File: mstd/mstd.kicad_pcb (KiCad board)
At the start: 2 copper layers, 80 x 96.2 mm, 89 parts, among them J1 PROG, J2 Barrel_Jack, Q1 SI2301CDS-T1-GE3, Q2 2N7002, SW1 TSX101G100-250, U1 ICE40UP5K-SG48ITR, U10 74HCT05, U12 74HCT4066, U2 TLV70212DBVR, U3 TMI6050-33, U4 ESP32-WROOM-32E-N16, U5 74LVX3245MTCX, U6 74LVX3245MTCX, U7 SSD1306 OLED, U8 74HCT05, U9 APX803S-31SA

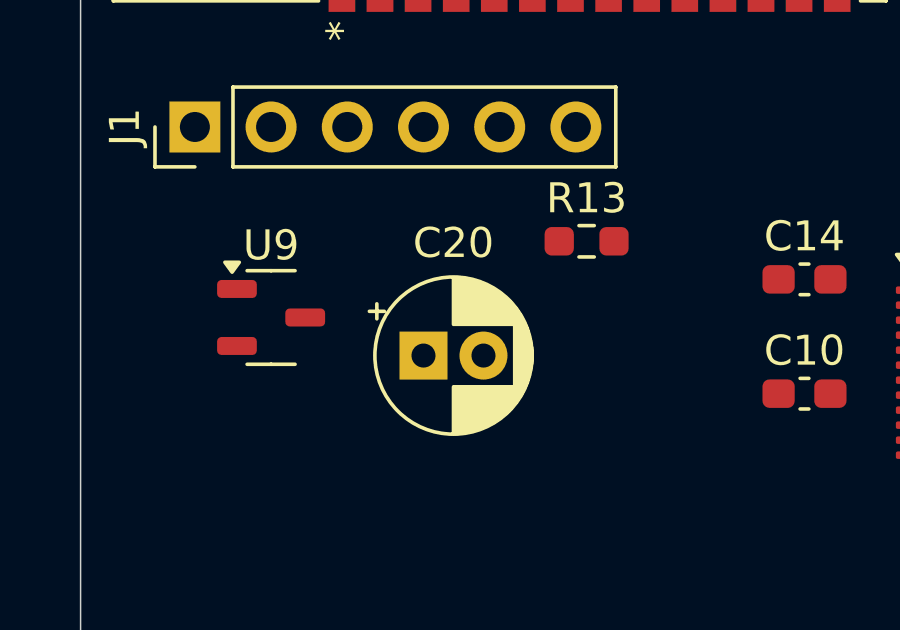
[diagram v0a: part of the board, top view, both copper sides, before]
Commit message: Changed reset capacitor to 1.0
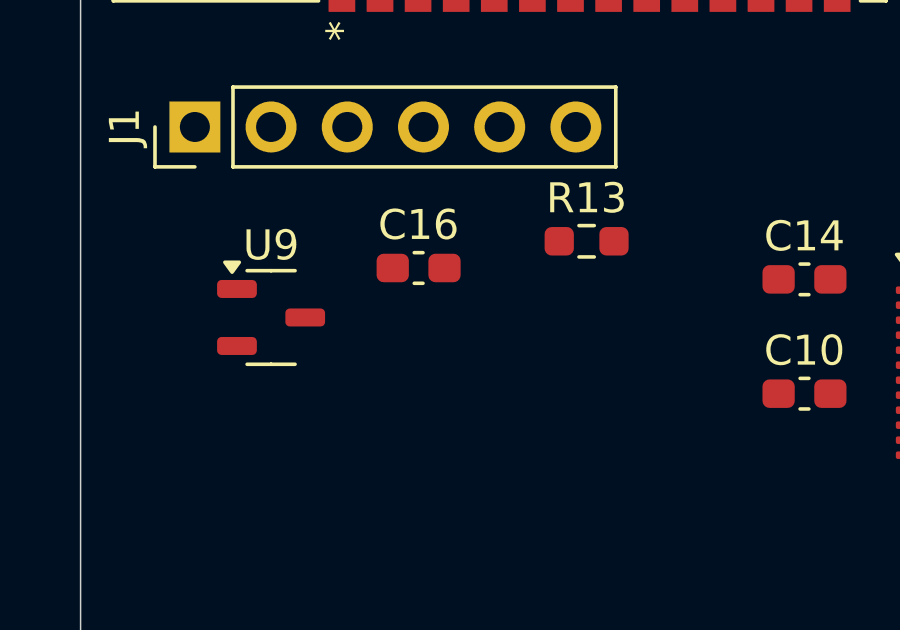
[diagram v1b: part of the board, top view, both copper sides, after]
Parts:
- removed C20: 10.0x16V, Capacitor_THT:CP_Radial_D5.0mm_P2.00mm
- added C16: 1.0, Capacitor_SMD:C_0603_1608Metric_Pad1.08x0.95mm_HandSolder, F.Cu at (63.3, 131.7)

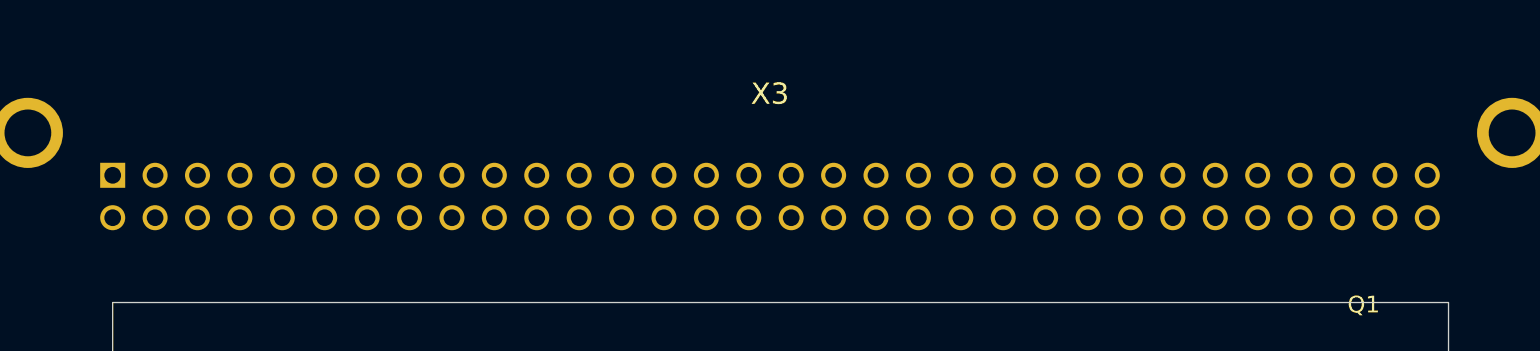
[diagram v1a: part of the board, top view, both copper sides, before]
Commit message: Update Harting connector pin numeration to match SNP
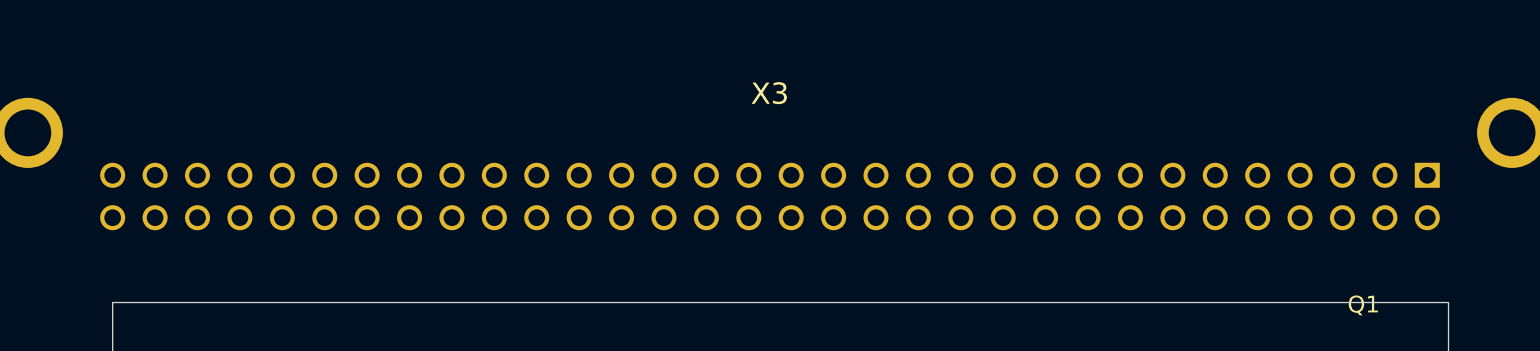
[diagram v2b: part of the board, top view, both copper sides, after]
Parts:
- X3: footprint local:09722642801 -> local:09722642801-1
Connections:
- X3 pad A32: unconnected-(X3D-ROM3-PadA32) -> (no net)
- X3 pad B32: /IO/DAL7 -> (no net)

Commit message: Routhing in finilizing stage
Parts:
- removed J2: Barrel_Jack, Connector_BarrelJack:BarrelJack_Wuerth_6941xx301002
- removed Q1: SI2301CDS-T1-GE3, easyeda2kicad:SOT-23-3_L3.0-W1.7-P0.95-LS2.9-BR
- removed R33: 1K, Resistor_SMD:R_0603_1608Metric_Pad0.98x0.95mm_HandSolder
- removed R34: 100K, Resistor_SMD:R_0603_1608Metric_Pad0.98x0.95mm_HandSolder
- added H1: MountingHole, MountingHole:MountingHole_3.2mm_M3_ISO14580, F.Cu at (116.8, 158.0)
- added H2: MountingHole, MountingHole:MountingHole_3.2mm_M3_ISO14580, F.Cu at (50.5, 101.1)
- added H3: MountingHole, MountingHole:MountingHole_3.2mm_M3_ISO14580, F.Cu at (139.6, 101.1)
- added H4: MountingHole, MountingHole:MountingHole_3.2mm_M3_ISO14580, F.Cu at (50.4, 168.5)
- added R40: 5K1, Resistor_SMD:R_0603_1608Metric_Pad0.98x0.95mm_HandSolder, F.Cu at (131.4, 143.2)
- added R41: 5K1, Resistor_SMD:R_0603_1608Metric_Pad0.98x0.95mm_HandSolder, F.Cu at (138.8, 142.3)
- added USB1: TYPEC-306DDW-ARP16, easyeda2kicad:USB-C-TH_TYPEC-306DDW-ARP16, F.Cu at (136.7, 142.7)
- C17, C22, C23, R3, R4, R5, R6, R7, R8, R9: moved to B.Cu
- moved R15 94.7 mm to (103.2, 110.2), turned to 180 degrees
- moved R30 91.9 mm to (101.3, 99.4), turned to 180 degrees
- moved R31 90.9 mm to (97.4, 99.4), turned to 180 degrees
- moved R32 90.0 mm to (67.1, 112.7), turned to 180 degrees
- moved R14 88.7 mm to (98.2, 110.8), turned to 90 degrees
- moved TP4 86.9 mm to (75.9, 112.7)
- moved TP3 83.6 mm to (75.9, 115.2)
- moved R29 80.2 mm to (92.2, 104.2), turned to 90 degrees
- moved TP2 80.0 mm to (76.9, 117.3)
- moved R19 77.3 mm to (89.9, 105.7), turned to -90 degrees
- moved R23 77.0 mm to (86.1, 112.1), turned to 180 degrees
- moved R16 75.2 mm to (98.2, 114.6), turned to -90 degrees
- moved C17 74.8 mm to (97.8, 104.6), turned to 180 degrees
- moved R28 73.2 mm to (90.5, 110.2), turned to -90 degrees
- moved R22 73.1 mm to (90.5, 121.0)
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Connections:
- R12 pad 1: /IO/ROM-CE3 -> /CE3
- R26 pad 1: /IO/WTB -> /WTB
- R28 pad 2: /IO/RUN -> /RUN
- R3 pad 1: /CPU/CIO7 -> /CPU/CIO2
- R32 pad 1: Net-(U1A-IOT_36b) -> /CPU/FIO4
- R4 pad 1: /CPU/CIO6 -> /CPU/CIO1
- R5 pad 1: /CPU/CIO0 -> /CPU/CI2
- R7 pad 1: /CPU/CI2 -> /CPU/CIO0
- SW1 pad 4: /CPU/CIO0 -> /CPU/CI2
- SW1 pad 6: /CPU/CI2 -> /CPU/CIO0
- TP1 pad 1: Net-(U1A-IOT_51a) -> Net-(U1A-IOT_36b)
- U1 pad 13: /CPU/FIO6 -> /RUN
- U1 pad 2: Net-(U1C-IOB_6a) -> /A6
- U1 pad 20: /CPU/FIO7 -> /CE3
- U1 pad 21: /CPU/FIO5 -> /WTB
- U1 pad 23: /IO/ROM-CE3 -> /IO/INIT
- U1 pad 26: /IO/DOUT -> /IO/ROM-CE2
- U1 pad 27: /IO/DIN -> /IO/ROM-CE1
- U1 pad 28: /IO/WTB -> /IO/IRQ
- U1 pad 3: Net-(U1C-IOB_9b) -> /A5
- U1 pad 32: /IO/ROM-CE1 -> /IO/DOUT
- U1 pad 34: /IO/ROM-CE2 -> /IO/DIN
- U1 pad 35: /IO/IRQ -> /IO/IAKN
- U1 pad 36: /IO/IAKN -> /A15
- U1 pad 38: /IO/INIT -> /A14
- U1 pad 4: Net-(U1C-IOB_8a) -> /A4
- U1 pad 42: Net-(U1A-IOT_51a) -> /A13
- U1 pad 43: /IO/RUN -> /A12
- U1 pad 48: Net-(U1C-IOB_4a) -> /A7
- U10 pad 12: /S-BK -> /IO/ROM-CE2
- U10 pad 13: Net-(X3C-INIT) -> Net-(X4D-CE2)
- U10 pad 2: /IO/ROM-CE3 -> /CE3
- U10 pad 3: /IO/RPLY -> Net-(X3A-WTBT)
- U10 pad 4: Net-(X3A-RPLY) -> /WTB
- U10 pad 8: /IO/IAKN -> /IO/ROM-CE1
- U10 pad 9: Net-(X3B-IAKN2) -> Net-(X4D-CE1)
- U12 pad 13: /IO/RUN -> /RUN
- U4 pad 10: /ROM-DIS2 -> /CPU/CIO2
- U4 pad 16: /S-BK -> /ROM-DIS1
- U4 pad 31: /CPU/CIO7 -> /ROM-DIS2
- U4 pad 33: /CPU/CIO6 -> /S-BK
- U4 pad 9: /ROM-DIS1 -> /CPU/CIO1
- U5 pad 10: /CPU/FIO7 -> /A7
- U5 pad 2: Net-(U1A-IOT_36b) -> /CPU/FIO4
- U5 pad 3: /CPU/FIO0 -> /CPU/FIO3
- U5 pad 4: /CPU/FIO1 -> /CPU/FIO2
- U5 pad 5: /CPU/FIO2 -> /CPU/FIO1
- U5 pad 6: /CPU/FIO3 -> /CPU/FIO0
- U5 pad 7: /CPU/FIO4 -> /A4
- U5 pad 8: /CPU/FIO5 -> /A5
- U5 pad 9: /CPU/FIO6 -> /A6
- U6 pad 10: Net-(U1C-IOB_9b) -> /A15
- U6 pad 2: Net-(U1A-IOT_36b) -> /CPU/FIO4
- U6 pad 3: Net-(U1C-IOB_0a) -> Net-(U1C-IOB_2a)
- U6 pad 4: Net-(U1C-IOB_2a) -> Net-(U1C-IOB_0a)
- U6 pad 5: Net-(U1C-IOB_3b_G6) -> Net-(U1C-IOB_5b)
- U6 pad 6: Net-(U1C-IOB_4a) -> Net-(U1C-IOB_3b_G6)
- U6 pad 7: Net-(U1C-IOB_5b) -> /A12
- U6 pad 8: Net-(U1C-IOB_6a) -> /A13
- U6 pad 9: Net-(U1C-IOB_8a) -> /A14
- U7 pad 3: /CPU/CIO6 -> /CPU/CIO1
- U7 pad 4: /CPU/CIO7 -> /CPU/CIO2
- U8 pad 1: Net-(X3A-SINC) -> Net-(X3B-IAKN2)
- U8 pad 10: /IO/ROM-CE1 -> /IO/DOUT
- U8 pad 11: Net-(X4D-CE1) -> Net-(X3A-DOUT)
- U8 pad 12: /IO/ROM-CE2 -> /IO/SYNC
- U8 pad 13: Net-(X4D-CE2) -> Net-(X3A-SINC)
- U8 pad 2: /IO/SYNC -> /IO/IAKN
- U8 pad 5: Net-(X3A-DOUT) -> Net-(X3C-INIT)
- U8 pad 6: /IO/DOUT -> /S-BK
- U8 pad 8: /IO/WTB -> Net-(X3A-RPLY)
- U8 pad 9: Net-(X3A-WTBT) -> /IO/RPLY
- X3 pad A32: (no net) -> unconnected-(X3D-ROM3-PadA32)
- X3 pad B32: (no net) -> /IO/DAL7
- X4 pad B16: (no net) -> /IO/DAL4
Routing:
- net +5V: track 0.00 -> 414.1 mm, vias 0 -> 15
- net +3V3: track 0.00 -> 395.6 mm, vias 0 -> 17
- net GND: track 0.00 -> 217.9 mm, vias 0 -> 61
- net /IO/DAL15: track 0.00 -> 153.2 mm, vias 0 -> 2
- net /IO/DAL13: track 0.00 -> 152.6 mm, vias 0 -> 1
- net /IO/DAL7: track 0.00 -> 151.2 mm, vias 0 -> 1
- net /IO/DAL14: track 0.00 -> 149.4 mm, vias 0 -> 1
- net /IO/DAL11: track 0.00 -> 146.0 mm, vias 0 -> 1
- net /IO/DAL0: track 0.00 -> 145.5 mm, vias 0 -> 1
- net /IO/DAL12: track 0.00 -> 145.3 mm, vias 0 -> 1
- net /IO/DAL2: track 0.00 -> 144.0 mm, vias 0 -> 1
- net Net-(X3A-DIN): track 0.00 -> 142.5 mm, vias 0 -> 2
- net /IO/DAL9: track 0.00 -> 141.0 mm, vias 0 -> 1
- net /IO/DAL1: track 0.97 -> 141.3 mm, vias 0 -> 1
- net /IO/DAL10: track 0.00 -> 139.3 mm, vias 0 -> 1
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- added copper zone on B.Cu, net GND
- added copper zone on F.Cu, net GND
- added copper zone on In1.Cu, net GND
- added copper zone on In2.Cu, net GND
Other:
- board size 80 x 96.2 mm -> 96 x 96.3 mm
- copper layers 2 -> 4
- rule pad_to_mask_clearance: 0.051 -> 0

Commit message: Routing finalized
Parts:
- R41: moved to B.Cu
- moved X4 1.23 mm to (81.0, 171.5)
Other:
- outline, holes or cut-outs redrawn
- board text added: "XVR-Product & Eduard Garanskij 2025 УКНЦ-БК МСТД+"

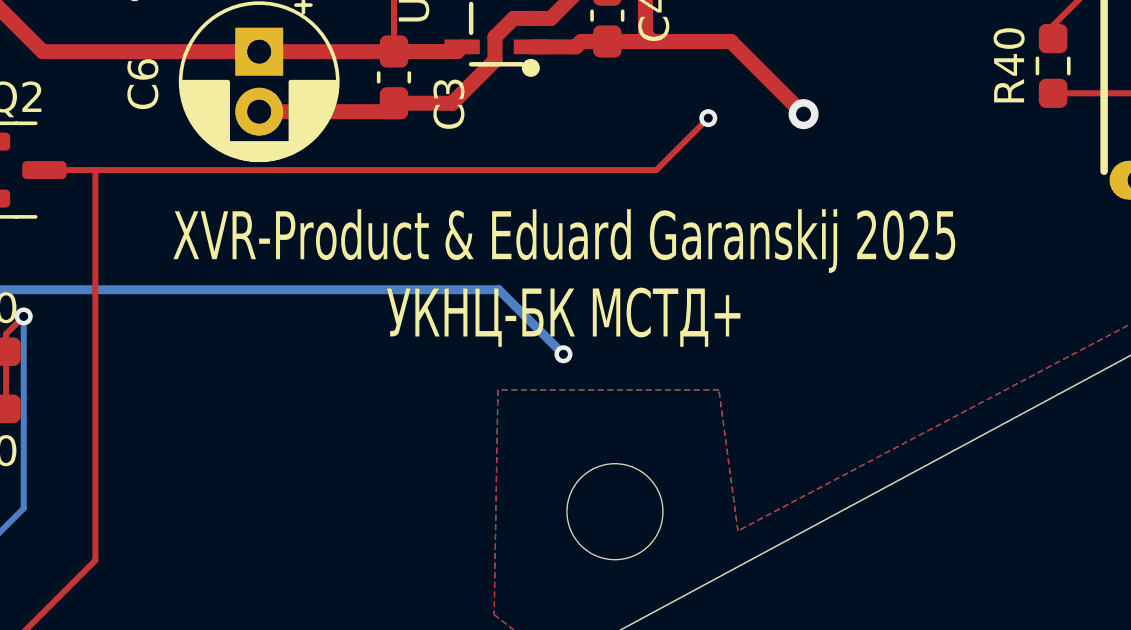
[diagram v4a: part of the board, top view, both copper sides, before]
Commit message: Added version on PCB
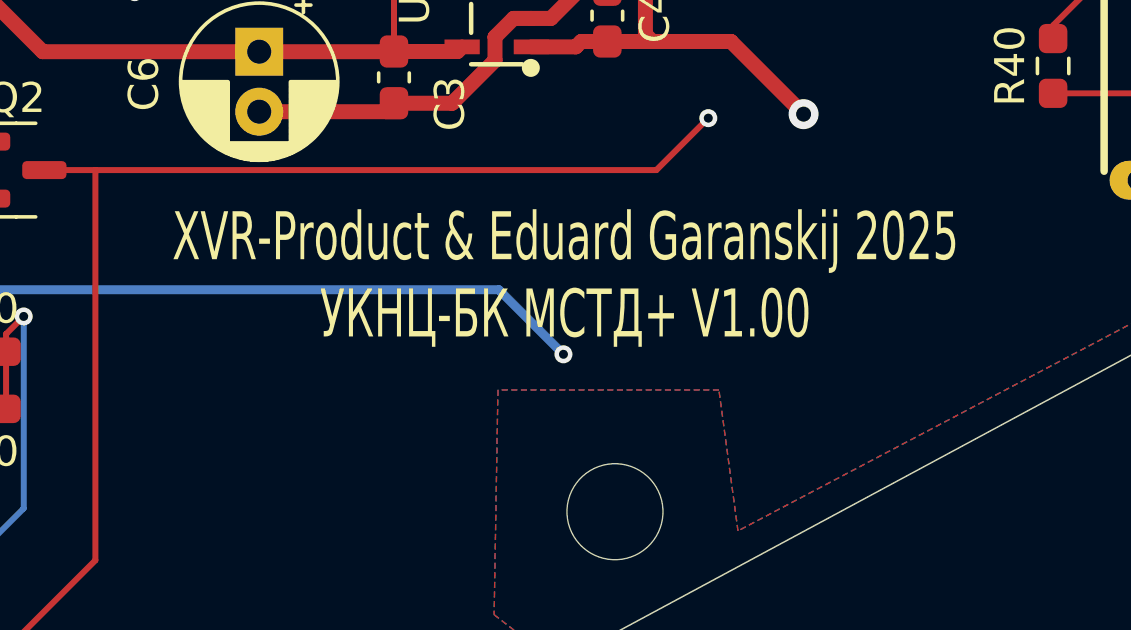
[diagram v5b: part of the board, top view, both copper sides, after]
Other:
- board text added: "XVR-Product & Eduard Garanskij 2025 УКНЦ-БК МСТД+ V1.00"
- board text removed: "XVR-Product & Eduard Garanskij 2025 УКНЦ-БК МСТД+"
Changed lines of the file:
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@@
 		(layer "Edge.Cuts")
 	)
-	(gr_text "XVR-Product & Eduard Garanskij 2025\nУКНЦ-БК МСТД+"
+	(gr_text "XVR-Product & Eduard Garanskij 2025\nУКНЦ-БК МСТД+ V1.00"
 		(at 115.19 150.17 0)
 		(layer "F.SilkS")

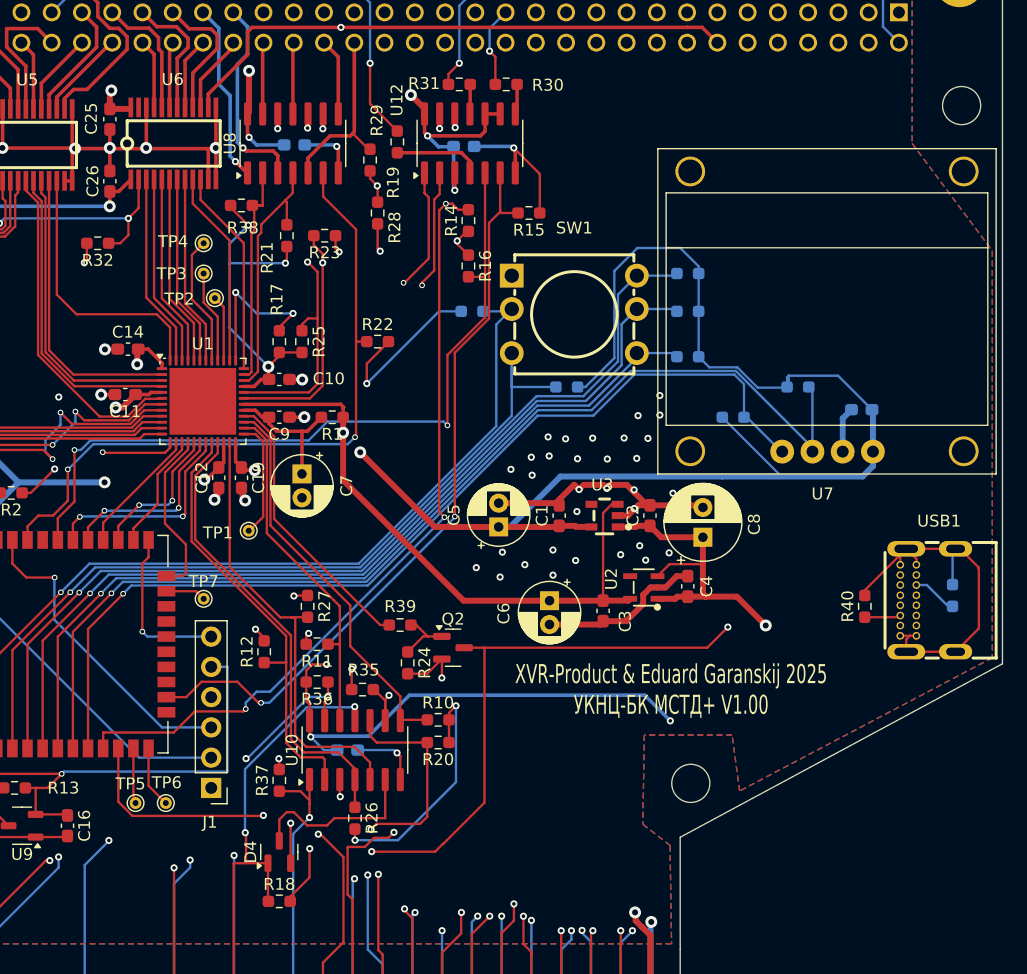
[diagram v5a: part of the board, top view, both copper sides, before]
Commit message: Added GND vias
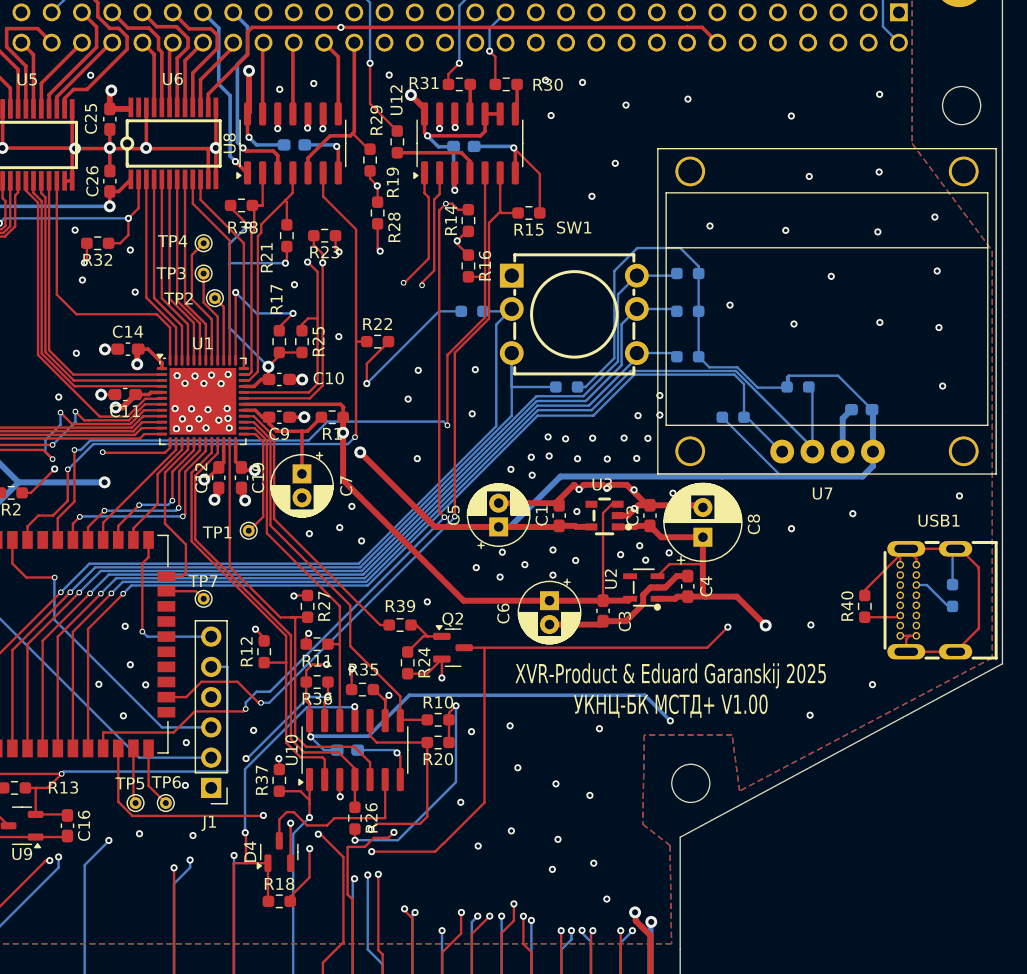
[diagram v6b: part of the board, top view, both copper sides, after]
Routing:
- net +3V3: track 395.6 -> 396.5 mm
- net GND: vias 61 -> 152
